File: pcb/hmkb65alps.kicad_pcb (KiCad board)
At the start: 2 copper layers, 305 x 103.4 mm, 157 parts, among them J1 AVR-ISP-6, J2 USB4105GFA120, SW1 SW_Push, SW10 SW_Push, SW11 SW_Push, SW12 SW_Push, SW13 SW_Push, SW14 SW_Push, SW15 SW_Push, SW16 SW_Push, SW17 SW_Push, SW18 SW_Push, SW19 SW_Push, SW2 SW_Push, SW20 SW_Push, SW21 SW_Push, SW22 SW_Push, SW23 SW_Push, SW24 SW_Push, SW25 SW_Push, SW26 SW_Push, SW27 SW_Push, SW28 SW_Push, SW29 SW_Push, SW3 SW_Push, SW30 SW_Push, SW31 SW_Push, SW32 SW_Push, SW33 SW_Push, SW34 SW_Push, SW35 SW_Push, SW36 SW_Push, SW37 SW_Push, SW38 SW_Push, SW39 SW_Push, SW4 SW_Push, SW40 SW_Push, SW41 SW_Push, SW42 SW_Push, SW43 SW_Push, SW44 SW_Push, SW45 SW_Push, SW46 SW_Push, SW47 SW_Push, SW48 SW_Push, SW49 SW_Push, SW5 SW_Push, SW50 SW_Push, SW51 SW_Push, SW52 SW_Push, SW53 SW_Push, SW54 SW_Push, SW55 SW_Push, SW56 SW_Push, SW57 SW_Push, SW58 SW_Push, SW59 SW_Push, SW6 SW_Push, SW60 SW_Push, SW61 SW_Push, SW62 SW_Push, SW63 SW_Push, SW64 SW_Push, SW65 SW_Push, SW66 SW_Push, SW67 SW_Push, SW68 SW_Push, SW69 SW_Push, SW7 SW_Push, SW8 SW_Push, SW9 SW_Push, U1 ATmega32U4-A, Y1 16MHz

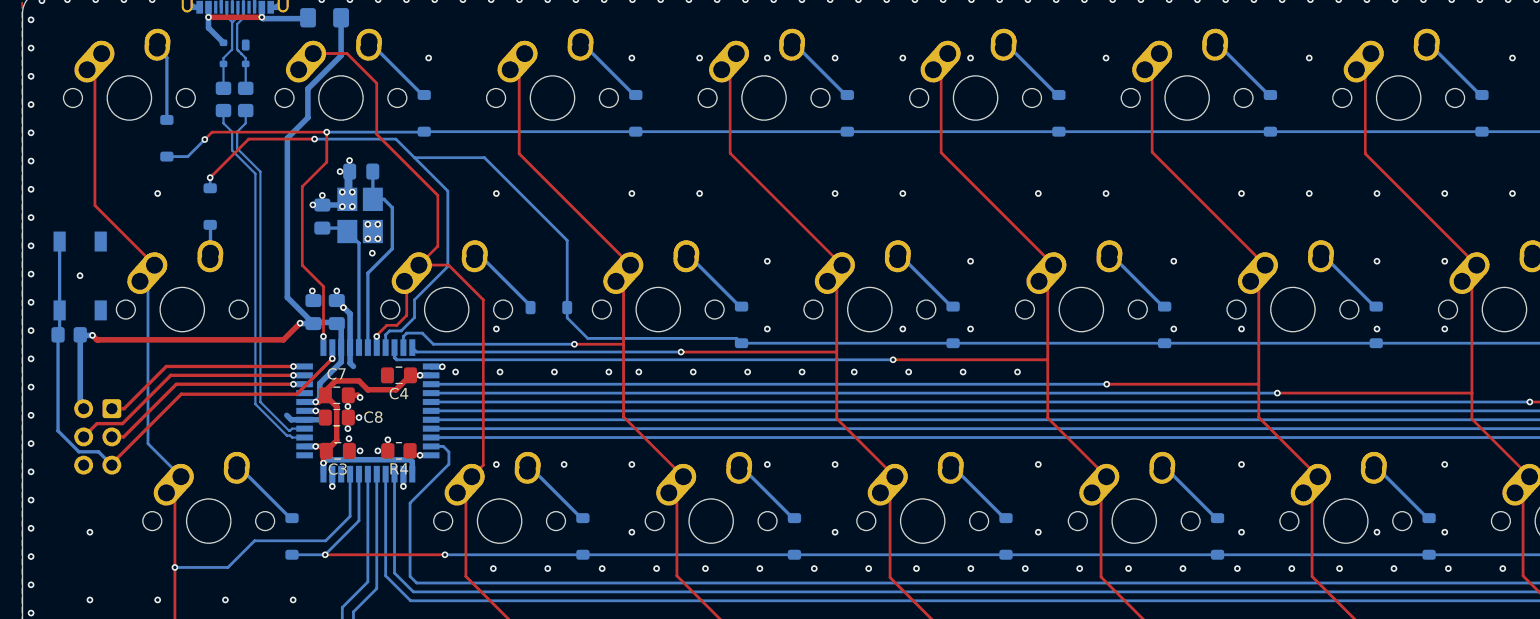
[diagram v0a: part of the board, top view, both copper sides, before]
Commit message: place some more stiching vias where it appeared reasonable
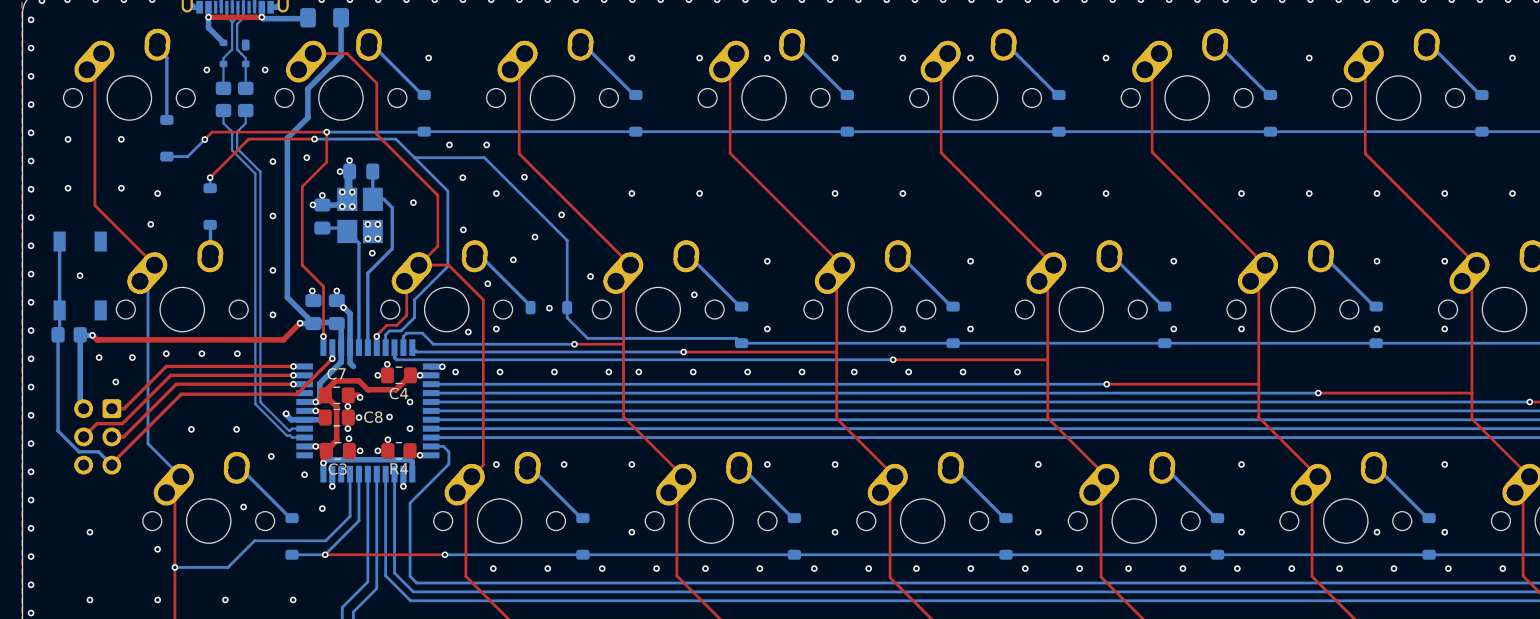
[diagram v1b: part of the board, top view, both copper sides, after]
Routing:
- net GND: track 23.5 -> 24.0 mm, vias 761 -> 806
